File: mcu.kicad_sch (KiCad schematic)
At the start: 6 parts, among them U3 ADAFRUIT_QT_PY

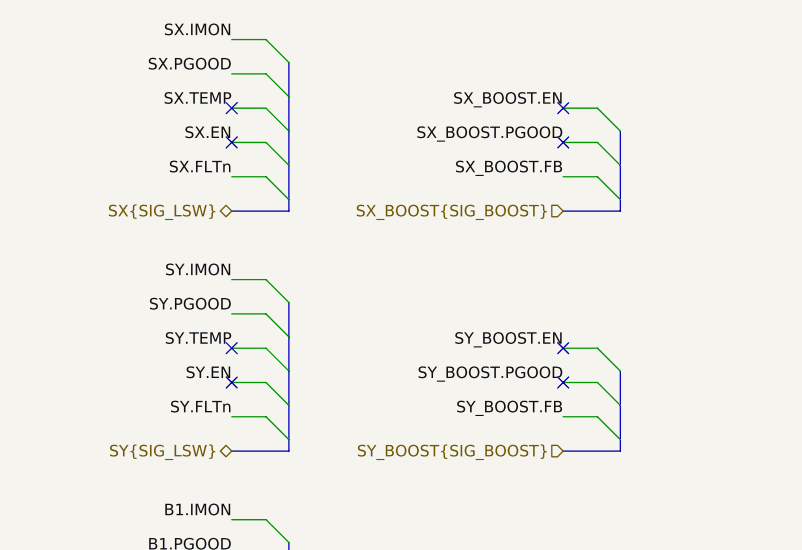
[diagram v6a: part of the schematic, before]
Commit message: Fixing circuit errors
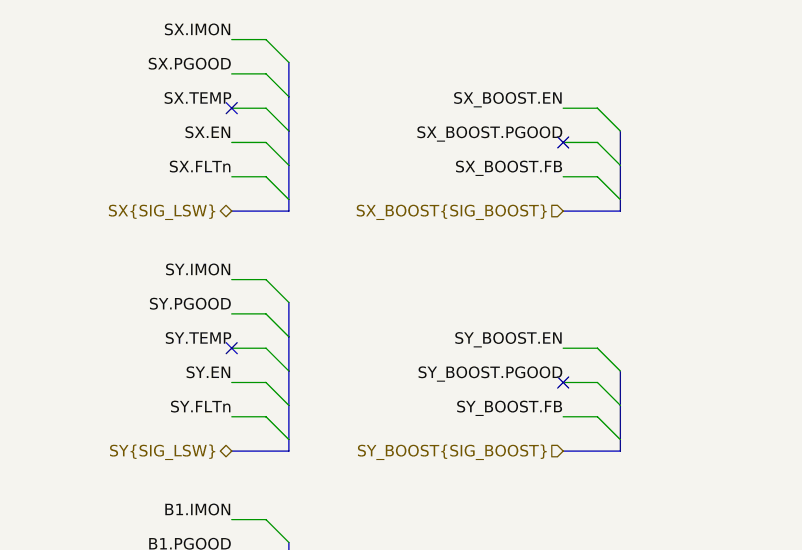
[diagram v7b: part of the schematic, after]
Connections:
- no-connect marks 16 -> 12
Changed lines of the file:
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@@
-	)
-	(no_connect
-		(at 80.01 66.04)
 	)
 	(no_connect
@@
 	)
 	(no_connect
-		(at 43.18 69.85)
-	)
-	(no_connect
-		(at 43.18 43.18)
-	)
-	(no_connect
 		(at 171.45 110.49)
 	)
@@
 		(at 43.18 39.37)
 	)
-	(no_connect
-		(at 80.01 39.37)
-	)
 	(bus_entry

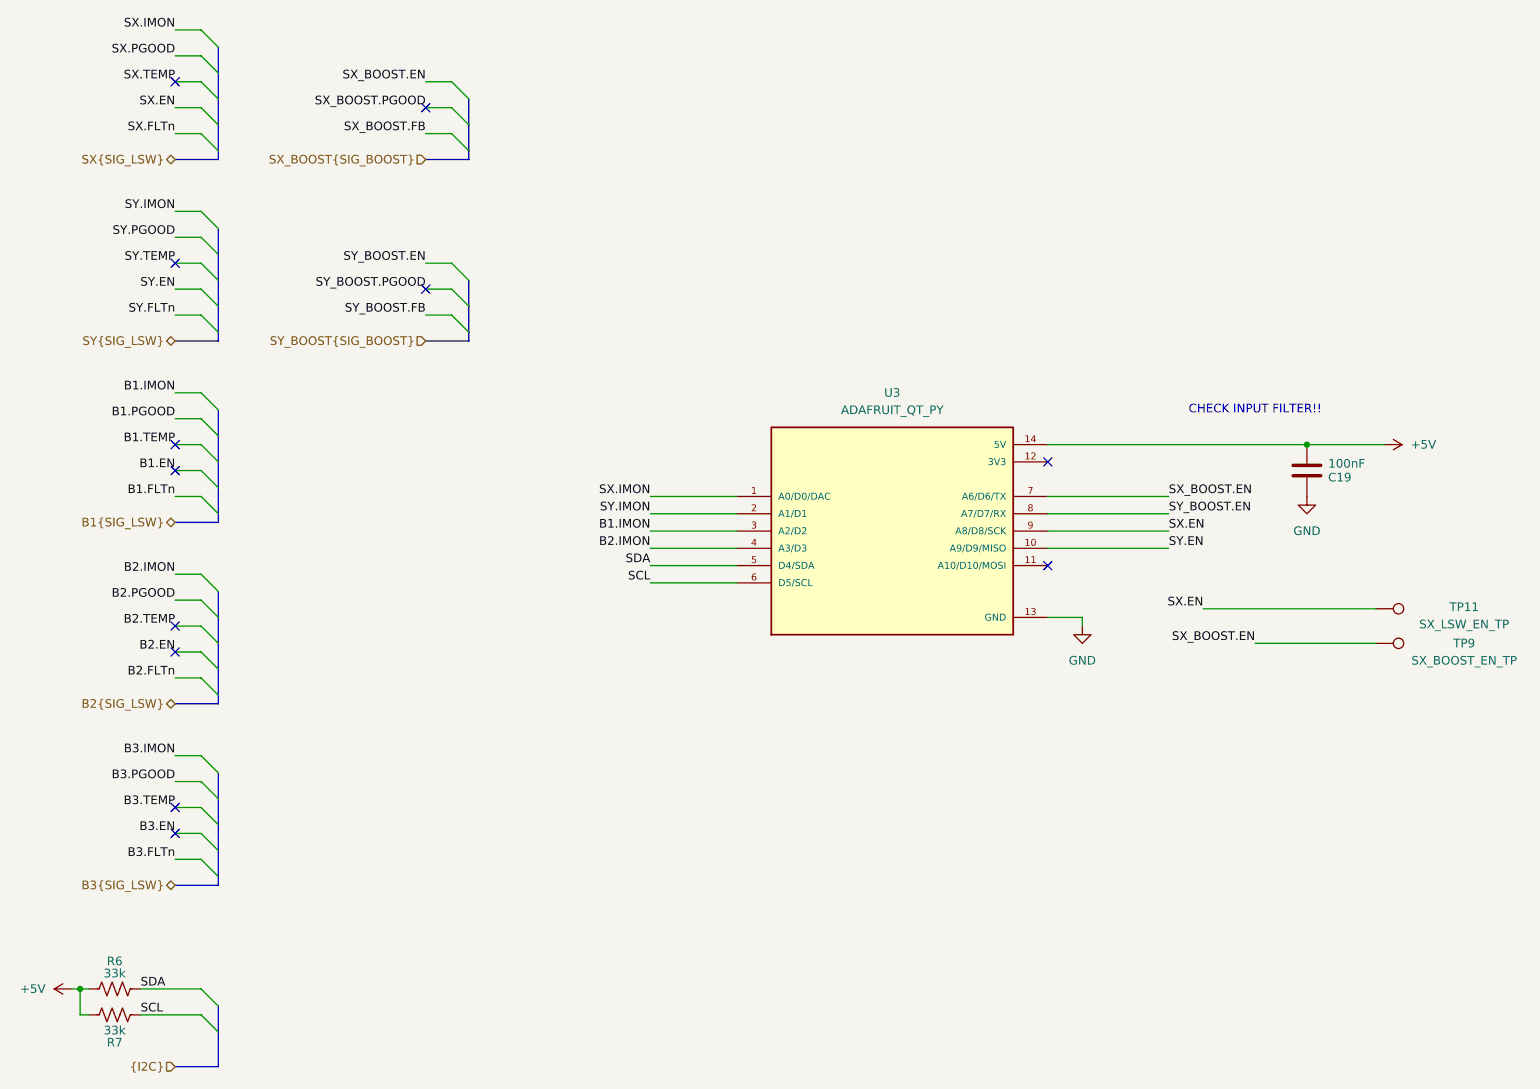
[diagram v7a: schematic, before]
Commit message: Most of frontend layout done. Still need to add in power and analog ground
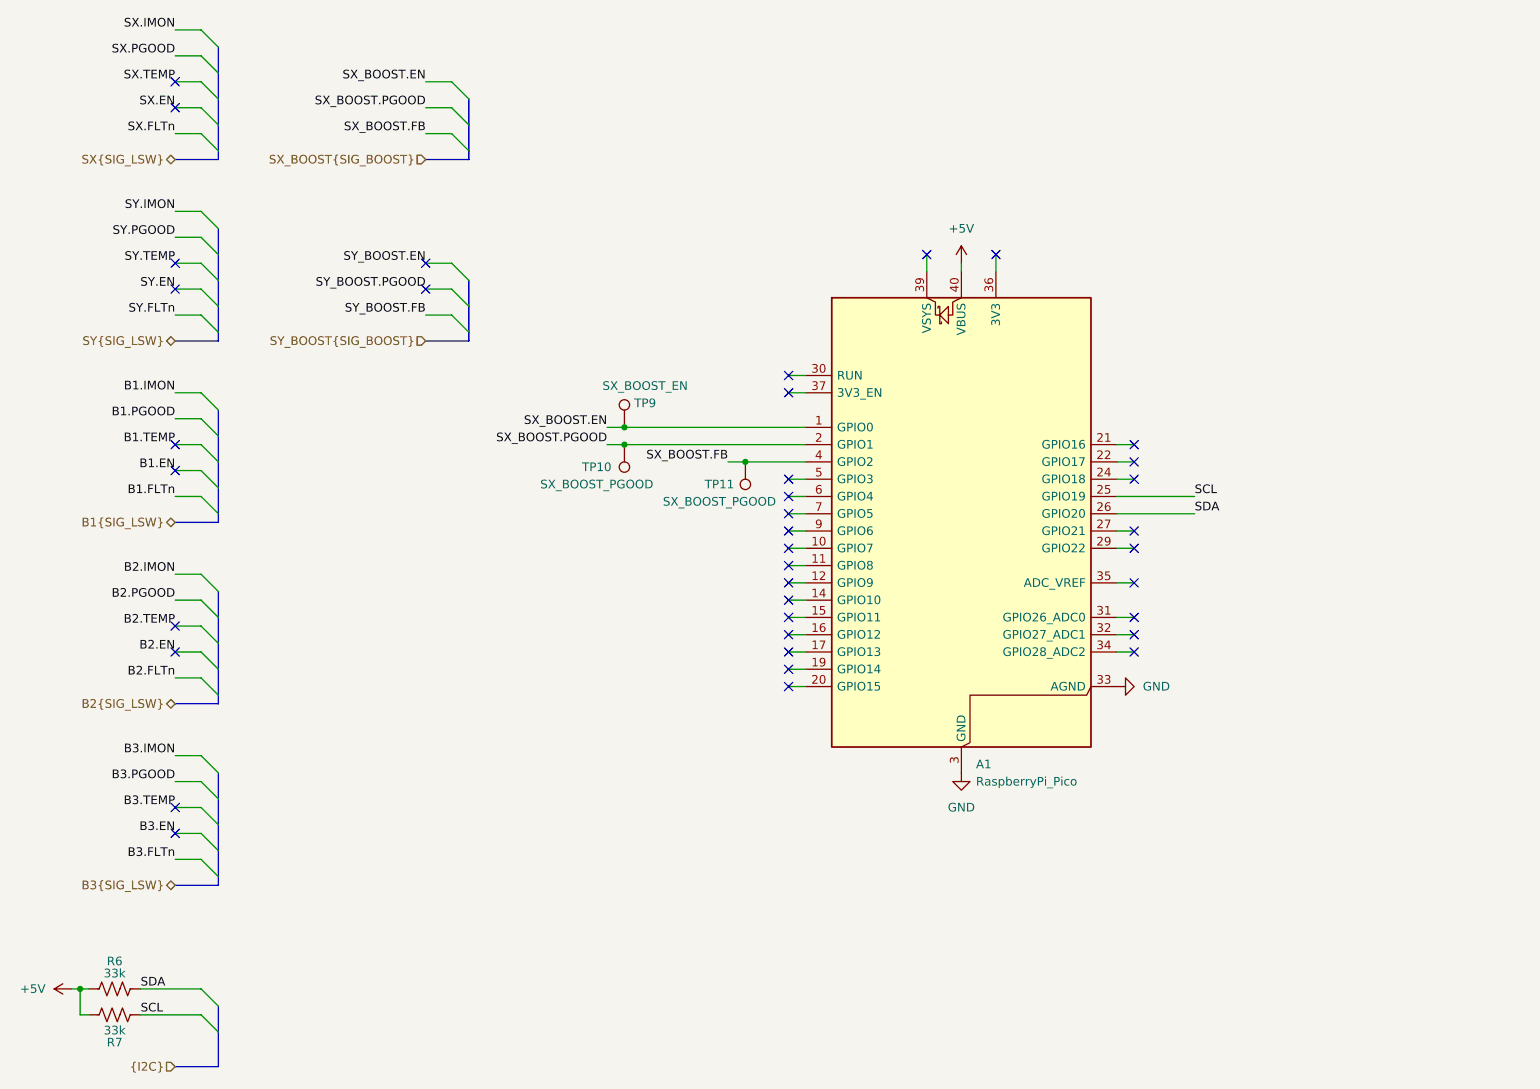
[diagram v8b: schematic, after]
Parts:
- removed C19: 100nF, Capacitor_SMD:C_1206_3216Metric, symbol Device:C
- removed U3: ADAFRUIT_QT_PY, _Power_Board:MODULE_ADAFRUIT_QT_PY, symbol _RP2040:ADAFRUIT_QT_PY
- added A1: RaspberryPi_Pico, Module:RaspberryPi_Pico_Common_Unspecified, symbol MCU_Module:RaspberryPi_Pico
- added TP10: SX_BOOST_PGOOD, symbol Connector:TestPoint
- TP11: value SX_LSW_EN_TP -> SX_BOOST_PGOOD
- TP9: value SX_BOOST_EN_TP -> SX_BOOST_EN
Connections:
- net +5V: now also A1.40 (VBUS)
- net GND: now also A1.13 (GND), A1.18 (GND), A1.23 (GND), A1.28 (GND), A1.3 (GND), A1.33 (AGND), A1.38 (GND), A1.8 (GND)
- net SCL: now also A1.25 (GPIO19)
- net SDA: now also A1.26 (GPIO20)
- net SX.EN: no longer TP11.1
- net SX_BOOST.EN: now also A1.1 (GPIO0)
- net SX_BOOST.FB: now also TP11.1, A1.4 (GPIO2)
- net SX_BOOST.PGOOD: now also A1.2 (GPIO1), TP10.1
- no-connect marks 12 -> 38
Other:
- note removed: "CHECK INPUT FILTER!!"
